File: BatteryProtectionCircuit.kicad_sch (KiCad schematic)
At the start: 26 parts, among them J1 Conn_01x07_Pin, K1 Relay_SPST-NC, Q1 NMOS, U1 LMC555xN, U2 LM358, U3 LM358, U4 ${SIM.PARAMS}

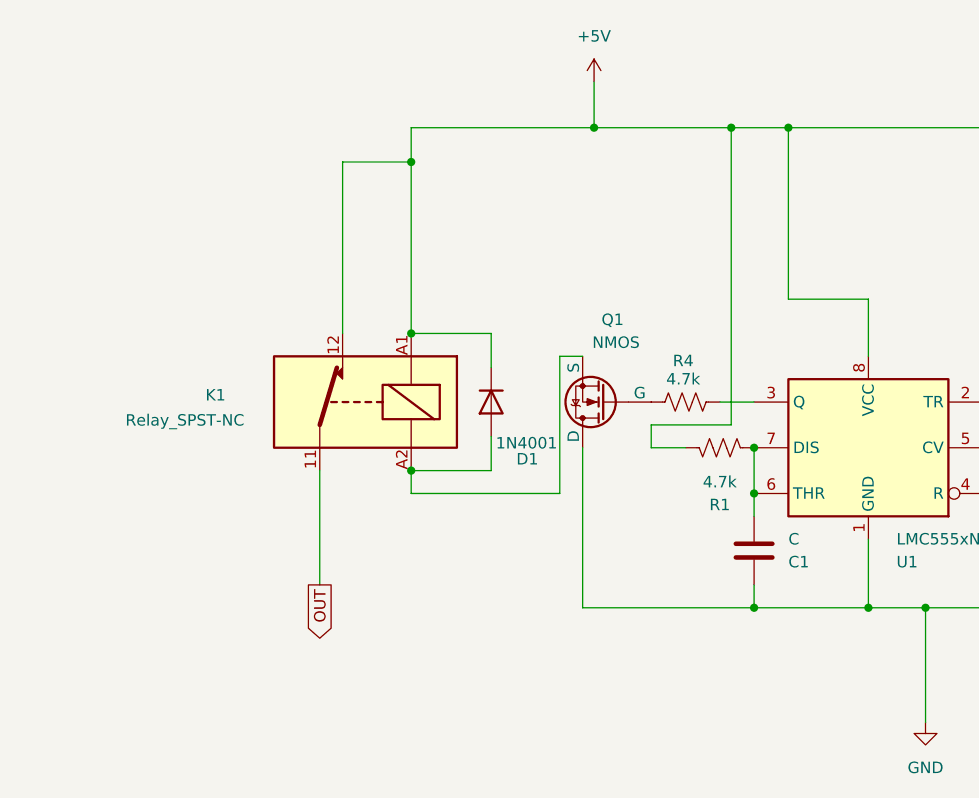
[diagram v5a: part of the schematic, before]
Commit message: Changed Relay to Latched Double Coil
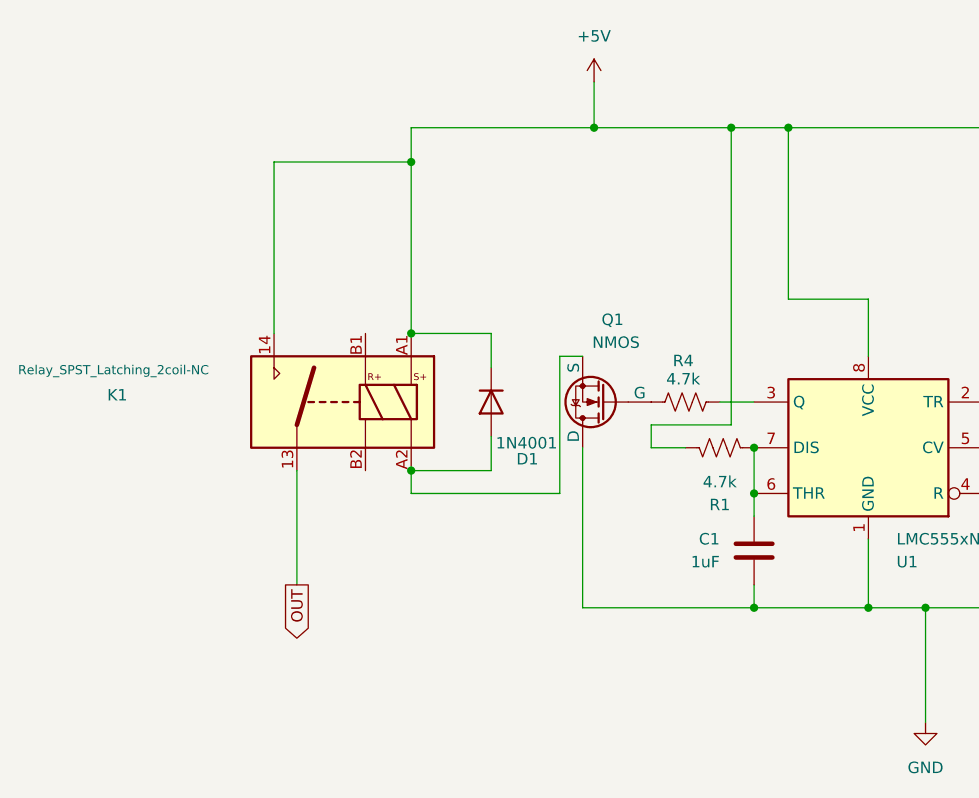
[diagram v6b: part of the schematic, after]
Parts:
- removed K1: Relay_SPST-NC, symbol Relay:Relay_SPST-NC
- added K1: Relay_SPST_Latching_2coil-NC, symbol Relay:Relay_SPST_Latching_2coil
- C1: value C -> 1uF
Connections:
- net +5V: now also K1.14, K1.A1
- net OUT: now also K1.13
- net at D1.2 (A), Q1.3 (S): now also K1.A2
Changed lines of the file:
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@@
 	)
 	(junction
-		(at 120.65 115.57)
+		(at 63.5 85.09)
 		(diameter 0)
 		(color 0 0 0 0)
 	)
 	(junction
-		(at 212.09 90.17)
+		(at 120.65 115.57)
 		(diameter 0)
 		(color 0 0 0 0)
 	)
 	(junction
-		(at 63.5 66.04)
+		(at 212.09 90.17)
 		(diameter 0)
 		(color 0 0 0 0)
@@
 	)
 	(junction
+		(at 63.5 100.33)
+		(diameter 0)
+		(color 0 0 0 0)
+	)
+	(junction
 		(at 101.6 102.87)
 		(diameter 0)
@@
 	)
 	(junction
-		(at 101.6 97.79)
+		(at 63.5 66.04)
 		(diameter 0)
 		(color 0 0 0 0)
 	)
 	(junction
-		(at 207.01 95.25)
+		(at 101.6 97.79)
 		(diameter 0)
 		(color 0 0 0 0)
 	)
 	(junction
-		(at 190.5 115.57)
+		(at 207.01 95.25)
 		(diameter 0)
 		(color 0 0 0 0)
 	)
 	(junction
-		(at 175.26 115.57)
+		(at 190.5 115.57)
 		(diameter 0)
 		(color 0 0 0 0)
 	)
 	(junction
-		(at 63.5 100.33)
+		(at 175.26 115.57)
 		(diameter 0)
 		(color 0 0 0 0)
@@
 	)
 	(junction
-		(at 63.5 85.09)
-		(diameter 0)
-		(color 0 0 0 0)
-	)
-	(junction
 		(at 83.82 62.23)
 		(diameter 0)
@@
 	(wire
 		(pts
-			(xy 55.88 66.04) (xy 55.88 85.09)
+			(xy 154.94 88.9) (xy 156.21 88.9)
 		)
 		(stroke
@@
 	(wire
 		(pts
-			(xy 154.94 88.9) (xy 156.21 88.9)
+			(xy 203.2 76.2) (xy 195.58 76.2)
 		)
 		(stroke
@@
 	(wire
 		(pts
-			(xy 203.2 76.2) (xy 195.58 76.2)
+			(xy 151.13 53.34) (xy 151.13 36.83)
 		)
 		(stroke
@@
 	(wire
 		(pts
-			(xy 151.13 53.34) (xy 151.13 36.83)
+			(xy 172.72 63.5) (xy 172.72 68.58)
 		)
 		(stroke
@@
 	(wire
 		(pts
-			(xy 172.72 63.5) (xy 172.72 68.58)
+			(xy 205.74 87.63) (xy 214.63 87.63)
 		)
 		(stroke
@@
 	(wire
 		(pts
-			(xy 205.74 87.63) (xy 214.63 87.63)
+			(xy 207.01 95.25) (xy 214.63 95.25)
 		)
 		(stroke
@@
 	(wire
 		(pts
-			(xy 207.01 95.25) (xy 214.63 95.25)
+			(xy 154.94 100.33) (xy 154.94 104.14)
 		)
 		(stroke
@@
 	(wire
 		(pts
-			(xy 154.94 100.33) (xy 154.94 104.14)
+			(xy 48.26 66.04) (xy 63.5 66.04)
 		)
 		(stroke
@@
 	(wire
 		(pts
-			(xy 55.88 66.04) (xy 63.5 66.04)
-		)
-		(stroke
-			(width 0)
-			(type default)
-		)
-	)
-	(wire
-		(pts
 			(xy 171.45 100.33) (xy 176.53 100.33)
 		)
@@
 	(wire
 		(pts
-			(xy 63.5 85.09) (xy 63.5 66.04)
-		)
-		(stroke
-			(width 0)
-			(type default)
-		)
-	)
-	(wire
-		(pts
 			(xy 212.09 60.96) (xy 212.09 90.17)
 		)
@@
 	(wire
 		(pts
+			(xy 63.5 66.04) (xy 63.5 85.09)
+		)
+		(stroke
+			(width 0)
+			(type default)
+		)
+	)
+	(wire
+		(pts
 			(xy 184.15 82.55) (xy 179.07 82.55)
 		)
@@
 	(wire
 		(pts
+			(xy 63.5 85.09) (xy 72.39 85.09)
+		)
+		(stroke
+			(width 0)
+			(type default)
+		)
+	)
+	(wire
+		(pts
 			(xy 154.94 100.33) (xy 156.21 100.33)
 		)
@@
 	(wire
 		(pts
-			(xy 63.5 85.09) (xy 72.39 85.09)
-		)
-		(stroke
-			(width 0)
-			(type default)
-		)
-	)
-	(wire
-		(pts
 			(xy 154.94 104.14) (xy 156.21 104.14)
 		)
@@
 	(wire
 		(pts
-			(xy 53.34 113.03) (xy 53.34 100.33)
+			(xy 195.58 88.9) (xy 201.93 88.9)
 		)
 		(stroke
@@
 	(wire
 		(pts
-			(xy 195.58 88.9) (xy 201.93 88.9)
+			(xy 203.2 95.25) (xy 207.01 95.25)
 		)
 		(stroke
@@
 	(wire
 		(pts
-			(xy 203.2 95.25) (xy 207.01 95.25)
+			(xy 170.18 92.71) (xy 163.83 92.71)
 		)
 		(stroke
@@
 	(wire
 		(pts
-			(xy 170.18 92.71) (xy 163.83 92.71)
+			(xy 201.93 36.83) (xy 214.63 36.83)
 		)
 		(stroke
@@
 	(wire
 		(pts
-			(xy 201.93 36.83) (xy 214.63 36.83)
+			(xy 50.8 100.33) (xy 50.8 113.03)
 		)
 		(stroke
@@
 	(wire
 		(pts
+			(xy 48.26 66.04) (xy 48.26 85.09)
+		)
+		(stroke
+			(width 0)
+			(type default)
+		)
+	)
+	(wire
+		(pts
 			(xy 101.6 115.57) (xy 114.3 115.57)
 		)
@@
 	(global_label "OUT"
 		(shape output)
-		(at 53.34 113.03 270)
+		(at 50.8 113.03 270)
 		(fields_autoplaced yes)
 		(effects
@@
 		)
 		(property "Intersheetrefs" "${INTERSHEET_REFS}"
-			(at 53.34 119.6438 90)
+			(at 50.8 119.6438 90)
 			(effects
 				(font
@@
 		(fields_autoplaced yes)
 		(property "Reference" "C1"
-			(at 105.41 110.4901 0)
+			(at 97.79 107.9499 0)
 			(effects
 				(font
 					(size 1.27 1.27)
 				)
-				(justify left)
+				(justify right)
 			)
 		)
-		(property "Value" "C"
-			(at 105.41 107.9501 0)
+		(property "Value" "1uF"
+			(at 97.79 110.4899 0)
 			(effects
 				(font
 					(size 1.27 1.27)
 				)
-				(justify left)
+				(justify right)
 			)
 		)
@@
 	)
 	(symbol
+		(lib_id "Relay:Relay_SPST_Latching_2coil")
+		(at 55.88 92.71 0)
+		(mirror y)
+		(unit 1)
+		(exclude_from_sim no)
+		(in_bom yes)
+		(on_board yes)
+		(dnp no)
+		(property "Reference" "K1"
+			(at 29.718 91.948 0)
+			(effects
+				(font
+					(size 1.27 1.27)
+				)
+				(justify right)
+			)
+		)
+		(property "Value" "Relay_SPST_Latching_2coil-NC"
+			(at 19.812 89.154 0)
+			(effects
+				(font
+					(size 1.016 1.016)
+				)
+				(justify right)
+			)
+		)
+		(property "Footprint" ""
+			(at 22.225 93.98 0)
+			(effects
+				(font
+					(size 1.27 1.27)
+				)
+				(hide yes)
+			)
+		)
+		(property "Datasheet" "~"
+			(at 55.88 92.71 0)
+			(effects
+				(font
+					(size 1.27 1.27)
+				)
+				(justify left)
+				(hide yes)
+			)
+		)
+		(property "Description" "Relay SPST, bistable, double-coil, EN50005"
+			(at 55.88 92.71 0)
+			(effects
+				(font
+					(size 1.27 1.27)
+				)
+				(hide yes)
+			)
+		)
+		(pin "13"
+		)
+		(pin "A1"
+		)
+		(pin "B2"
+		)
+		(pin "A2"
+		)
+		(pin "B1"
+		)
+		(pin "14"
+		)
+		(instances
+			(project ""
+				(path "/299dddd9-ac06-42a6-950e-710b9bcf8f9e"
+					(reference "K1")
+					(unit 1)
+				)
+			)
+		)
+	)
+	(symbol
 		(lib_id "Device:D")
 		(at 160.02 104.14 0)
@@
 				)
 			)
-		)
-	)
-	(symbol
-		(lib_id "Relay:Relay_SPST-NC")
-		(at 58.42 92.71 0)
-		(mirror y)
-		(unit 1)
-		(exclude_from_sim no)
-		(in_bom yes)
-		(on_board yes)
-		(dnp no)
-		(property "Reference" "K1"
-			(at 40.64 91.948 0)
-			(effects
-				(font
-					(size 1.27 1.27)
-				)
-				(justify right)
-			)
-		)
-		(property "Value" "Relay_SPST-NC"
-			(at 31.75 94.742 0)
-			(effects
-				(font
-					(size 1.27 1.27)
-				)
-				(justify right)
-			)
-		)
-		(property "Footprint" ""
-			(at 46.99 93.98 0)
-			(effects
-				(font
-					(size 1.27 1.27)
-				)
-				(justify left)
-				(hide yes)
-			)
-		)
-		(property "Datasheet" "~"
-			(at 58.42 92.71 0)
-			(effects
-				(font
-					(size 1.27 1.27)
-				)
-				(hide yes)
-			)
-		)
-		(property "Description" "Relay SPST, normally closed, EN50005"
-			(at 58.42 92.71 0)
-			(effects
-				(font
-					(size 1.27 1.27)
-				)
-				(hide yes)
-			)
-		)
-		(pin "A1"
-		)
-		(pin "12"
-		)
-		(pin "11"
-		)
-		(pin "A2"
-		)
-		(instances
-			(project ""
-				(path "/299dddd9-ac06-42a6-950e-710b9bcf8f9e"
-					(reference "K1")
-					(unit 1)
-				)
-			)

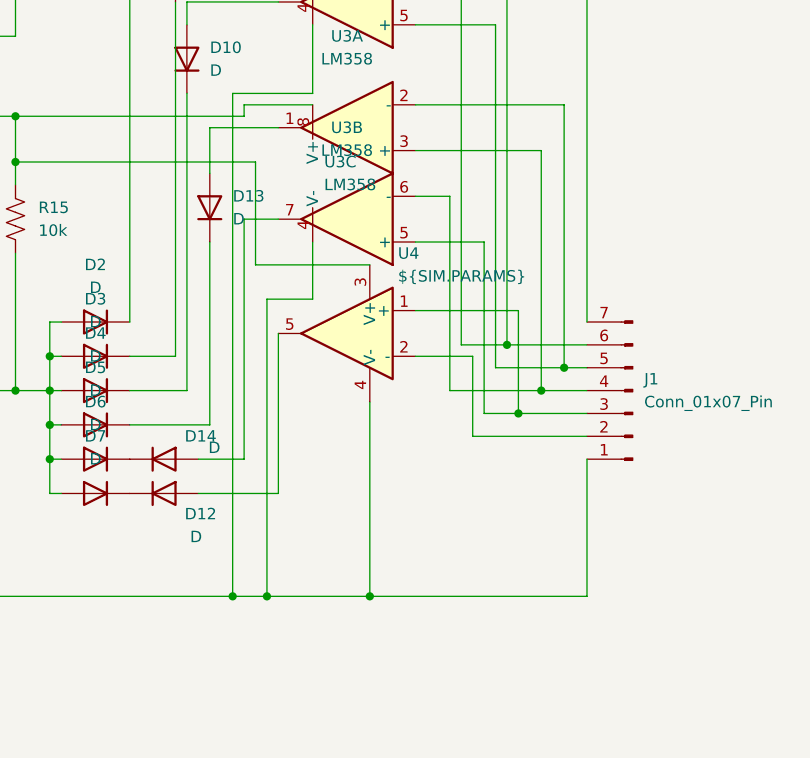
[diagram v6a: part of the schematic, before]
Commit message: Added footprints for all components
Besides relay
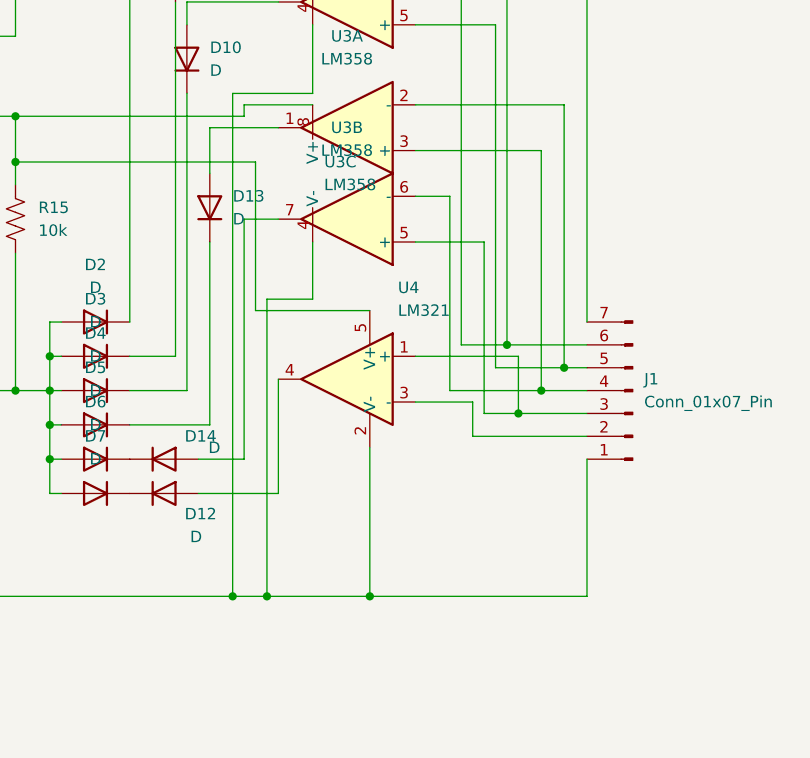
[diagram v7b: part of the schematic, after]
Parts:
- removed U4: ${SIM.PARAMS}, symbol Simulation_SPICE:OPAMP
- added U4: LM321, Package_TO_SOT_SMD:SOT-23-5, symbol Amplifier_Operational:LM321
- C1: footprint (none) -> Capacitor_SMD:C_0805_2012Metric
- D10, D12, D13, D2, D3, D4, D5, D6, D7, D8, D9: footprint (none) -> Diode_SMD:D_0805_2012Metric
- D14: footprint (none) -> Connector_PinHeader_1.00mm:PinHeader_1x02_P1.00mm_Vertical_SMD_Pin1Left
- Q1: footprint (none) -> Package_TO_SOT_SMD:SOT-23
- R1, R15, R2, R3, R4: footprint (none) -> Resistor_SMD:R_0805_2012Metric
- U2, U3: footprint (none) -> Package_DIP:DIP-8_W7.62mm
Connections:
- net +5V: now also U4.5 (V+)
- net GND: now also U4.2 (V-)
- net at J1.3 (Pin_3), U3.5 (+): now also U4.1 (+)
- net at J1.2 (Pin_2): now also U4.3 (-)
- net at D12.2 (A): now also U4.4
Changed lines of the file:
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@@
 	(wire
 		(pts
-			(xy 180.34 86.36) (xy 180.34 104.14)
+			(xy 180.34 91.44) (xy 180.34 104.14)
 		)
 		(stroke
@@
 	(wire
 		(pts
-			(xy 207.01 95.25) (xy 207.01 83.82)
-		)
-		(stroke
-			(width 0)
-			(type default)
-		)
-	)
-	(wire
-		(pts
-			(xy 190.5 78.74) (xy 177.8 78.74)
+			(xy 207.01 88.9) (xy 207.01 95.25)
+		)
+		(stroke
+			(width 0)
+			(type default)
+		)
+	)
+	(wire
+		(pts
+			(xy 190.5 83.82) (xy 177.8 83.82)
 		)
 		(stroke
@@
 	(wire
 		(pts
-			(xy 177.8 78.74) (xy 177.8 67.31)
+			(xy 177.8 83.82) (xy 177.8 67.31)
 		)
 		(stroke
@@
 	(wire
 		(pts
-			(xy 207.01 83.82) (xy 195.58 83.82)
+			(xy 207.01 88.9) (xy 195.58 88.9)
 		)
 		(stroke
@@
 	(wire
 		(pts
-			(xy 190.5 93.98) (xy 190.5 115.57)
-		)
-		(stroke
-			(width 0)
-			(type default)
-		)
-	)
-	(wire
-		(pts
-			(xy 195.58 88.9) (xy 201.93 88.9)
+			(xy 190.5 99.06) (xy 190.5 115.57)
+		)
+		(stroke
+			(width 0)
+			(type default)
+		)
+	)
+	(wire
+		(pts
+			(xy 195.58 93.98) (xy 201.93 93.98)
 		)
 		(stroke
@@
 	(wire
 		(pts
-			(xy 201.93 97.79) (xy 201.93 88.9)
+			(xy 201.93 93.98) (xy 201.93 97.79)
 		)
 		(stroke
@@
 			)
 		)
-		(property "Footprint" ""
+		(property "Footprint" "Package_DIP:DIP-8_W7.62mm"
 			(at 187.96 73.66 0)
 			(effects
@@
 					(reference "U3")
 					(unit 2)
+				)
+			)
+		)
+	)
+	(symbol
+		(lib_id "Amplifier_Operational:LM321")
+		(at 187.96 91.44 0)
+		(mirror y)
+		(unit 1)
+		(exclude_from_sim no)
+		(in_bom yes)
+		(on_board yes)
+		(dnp no)
+		(fields_autoplaced yes)
+		(property "Reference" "U4"
+			(at 193.6181 81.28 0)
+			(effects
+				(font
+					(size 1.27 1.27)
+				)
+				(justify right)
+			)
+		)
+		(property "Value" "LM321"
+			(at 193.6181 83.82 0)
+			(effects
+				(font
+					(size 1.27 1.27)
+				)
+				(justify right)
+			)
+		)
+		(property "Footprint" "Package_TO_SOT_SMD:SOT-23-5"
+			(at 187.96 91.44 0)
+			(effects
+				(font
+					(size 1.27 1.27)
+				)
+				(hide yes)
+			)
+		)
+		(property "Datasheet" "http://www.ti.com/lit/ds/symlink/lm321.pdf"
+			(at 187.96 91.44 0)
+			(effects
+				(font
+					(size 1.27 1.27)
+				)
+				(hide yes)
+			)
+		)
+		(property "Description" "Low Power Single Operational Amplifier, SOT-23-5"
+			(at 187.96 91.44 0)
+			(effects
+				(font
+					(size 1.27 1.27)
+				)
+				(hide yes)
+			)
+		)
+		(pin "5"
+		)
+		(pin "3"
+		)
+		(pin "2"
+		)
+		(pin "4"
+		)
+		(pin "1"
+		)
+		(instances
+			(project ""
+				(path "/299dddd9-ac06-42a6-950e-710b9bcf8f9e"
+					(reference "U4")
+					(unit 1)
 				)
 			)
@@
 			)
 		)
-		(property "Footprint" ""
+		(property "Footprint" "Connector_PinHeader_1.00mm:PinHeader_1x02_P1.00mm_Vertical_SMD_Pin1Left"
 			(at 167.64 100.33 0)
 			(effects
@@
 			)
 		)
-		(property "Footprint" ""
+		(property "Footprint" "Package_DIP:DIP-8_W7.62mm"
 			(at 187.96 49.53 0)
 			(effects
@@
 			)
 		)
-		(property "Footprint" ""
+		(property "Footprint" "Resistor_SMD:R_0805_2012Metric"
 			(at 98.044 98.806 90)
 			(effects
@@
 				(path "/299dddd9-ac06-42a6-950e-710b9bcf8f9e"
 					(reference "R1")
-					(unit 1)
-				)
-			)
-		)
-	)
-	(symbol
-		(lib_id "Simulation_SPICE:OPAMP")
-		(at 187.96 86.36 0)
-		(mirror y)
-		(unit 1)
-		(exclude_from_sim no)
-		(in_bom yes)
-		(on_board yes)
-		(dnp no)
-		(fields_autoplaced yes)
-		(property "Reference" "U4"
-			(at 193.6181 77.47 0)
-			(effects
-				(font
-					(size 1.27 1.27)
-				)
-				(justify right)
-			)
-		)
-		(property "Value" "${SIM.PARAMS}"
-			(at 193.6181 80.01 0)
-			(effects
-				(font
-					(size 1.27 1.27)
-				)
-				(justify right)
-			)
-		)
-		(property "Footprint" ""
-			(at 187.96 86.36 0)
-			(effects
-				(font
-					(size 1.27 1.27)
-				)
-				(hide yes)
-			)
-		)
-		(property "Datasheet" "https://ngspice.sourceforge.io/docs/ngspice-html-manual/manual.xhtml#sec__SUBCKT_Subcircuits"
-			(at 187.96 86.36 0)
-			(effects
-				(font
-					(size 1.27 1.27)
-				)
-				(hide yes)
-			)
-		)
-		(property "Description" "Operational amplifier, single"
-			(at 187.96 86.36 0)
-			(effects
-				(font
-					(size 1.27 1.27)
-				)
-				(hide yes)
-			)
-		)
-		(property "Sim.Pins" "1=in+ 2=in- 3=vcc 4=vee 5=out"
-			(at 187.96 86.36 0)
-			(effects
-				(font
-					(size 1.27 1.27)
-				)
-				(hide yes)
-			)
-		)
-		(property "Sim.Device" "SUBCKT"
-			(at 187.96 86.36 0)
-			(effects
-				(font
-					(size 1.27 1.27)
-				)
-				(justify left)
-				(hide yes)
-			)
-		)
-		(property "Sim.Library" "${KICAD9_SYMBOL_DIR}/Simulation_SPICE.sp"
-			(at 187.96 86.36 0)
-			(effects
-				(font
-					(size 1.27 1.27)
-				)
-				(hide yes)
-			)
-		)
-		(property "Sim.Name" "kicad_builtin_opamp"
-			(at 187.96 86.36 0)
-			(effects
-				(font
-					(size 1.27 1.27)
-				)
-				(hide yes)
-			)
-		)
-		(pin "4"
-		)
-		(pin "2"
-		)
-		(pin "1"
-		)
-		(pin "3"
-		)
-		(pin "5"
-		)
-		(instances
-			(project ""
-				(path "/299dddd9-ac06-42a6-950e-710b9bcf8f9e"
-					(reference "U4")
 					(unit 1)
 				)
@@
 			)
 		)
-		(property "Footprint" ""
+		(property "Footprint" "Diode_SMD:D_0805_2012Metric"
 			(at 163.83 43.18 0)
 			(effects
@@
 			)
 		)
-		(property "Footprint" ""
+		(property "Footprint" "Diode_SMD:D_0805_2012Metric"
 			(at 160.02 85.09 0)
 			(effects
@@
 			)
 		)
-		(property "Footprint" ""
+		(property "Footprint" "Resistor_SMD:R_0805_2012Metric"
 			(at 134.366 98.806 90)
 			(effects
@@
 			)
 		)
-		(property "Footprint" ""
+		(property "Footprint" "Diode_SMD:D_0805_2012Metric"
 			(at 160.02 96.52 0)
 			(effects
@@
 			)
 		)
-		(property "Footprint" ""
+		(property "Footprint" "Diode_SMD:D_0805_2012Metric"
 			(at 172.72 72.39 0)
 			(effects
@@
 			)
 		)
-		(property "Footprint" ""
+		(property "Footprint" "Diode_SMD:D_0805_2012Metric"
 			(at 160.02 92.71 0)
 			(effects
@@
 			)
 		)
-		(property "Footprint" ""
+		(property "Footprint" "Capacitor_SMD:C_0805_2012Metric"
 			(at 102.5652 105.41 0)
 			(effects
@@
 			)
 		)
-		(property "Footprint" ""
+		(property "Footprint" "Resistor_SMD:R_0805_2012Metric"
 			(at 93.726 93.726 90)
 			(effects
@@
 			)
 		)
-		(property "Footprint" ""
+		(property "Footprint" "Resistor_SMD:R_0805_2012Metric"
 			(at 152.146 73.914 90)
 			(effects
@@
 			)
 		)
-		(property "Footprint" ""
+		(property "Footprint" "Package_DIP:DIP-8_W7.62mm"
 			(at 187.96 63.5 0)
 			(effects
@@
 			)
 		)
-		(property "Footprint" ""
+		(property "Footprint" "Diode_SMD:D_0805_2012Metric"
 			(at 160.02 104.14 0)
 			(effects
@@
 			)
 		)
-		(property "Footprint" ""
+		(property "Footprint" "Diode_SMD:D_0805_2012Metric"
 			(at 170.18 55.88 0)
 			(effects
@@
 			)
 		)
-		(property "Footprint" ""
+		(property "Footprint" "Diode_SMD:D_0805_2012Metric"
 			(at 167.64 104.14 0)
 			(effects
@@
 			)
 		)
-		(property "Footprint" ""
+		(property "Footprint" "Diode_SMD:D_0805_2012Metric"
 			(at 160.02 88.9 0)
 			(effects
@@
 			)
 		)
-		(property "Footprint" ""
+		(property "Footprint" "Diode_SMD:D_0805_2012Metric"
 			(at 168.91 45.72 0)
 			(effects
@@
 			)
 		)
-		(property "Footprint" ""
+		(property "Footprint" "Diode_SMD:D_0805_2012Metric"
 			(at 160.02 100.33 0)
 			(effects
@@
 			)
 		)
-		(property "Footprint" ""
+		(property "Footprint" "Package_DIP:DIP-8_W7.62mm"
 			(at 186.69 68.58 0)
 			(effects
@@
 			)
 		)
-		(property "Footprint" ""
+		(property "Footprint" "Package_TO_SOT_SMD:SOT-23"
 			(at 80.01 95.25 0)
 			(effects
@@
 			)
 		)
-		(property "Footprint" ""
+		(property "Footprint" "Package_DIP:DIP-8_W7.62mm"
 			(at 187.96 39.37 0)
 			(effects
@@
 			)
 		)
-		(property "Footprint" ""
+		(property "Footprint" "Package_DIP:DIP-8_W7.62mm"
 			(at 186.69 44.45 0)
 			(effects
@@
 			)
 		)
-		(property "Footprint" ""
+		(property "Footprint" "Resistor_SMD:R_0805_2012Metric"
 			(at 143.764 93.726 90)
 			(effects
